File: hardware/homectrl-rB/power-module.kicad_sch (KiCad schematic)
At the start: 36 parts, among them J1 Barrel_Jack, Q1 DMP6023LE-13, U2 TPS5405DR, U3 ID_LM66100DCKR, U4 ID_LM66100DCKR

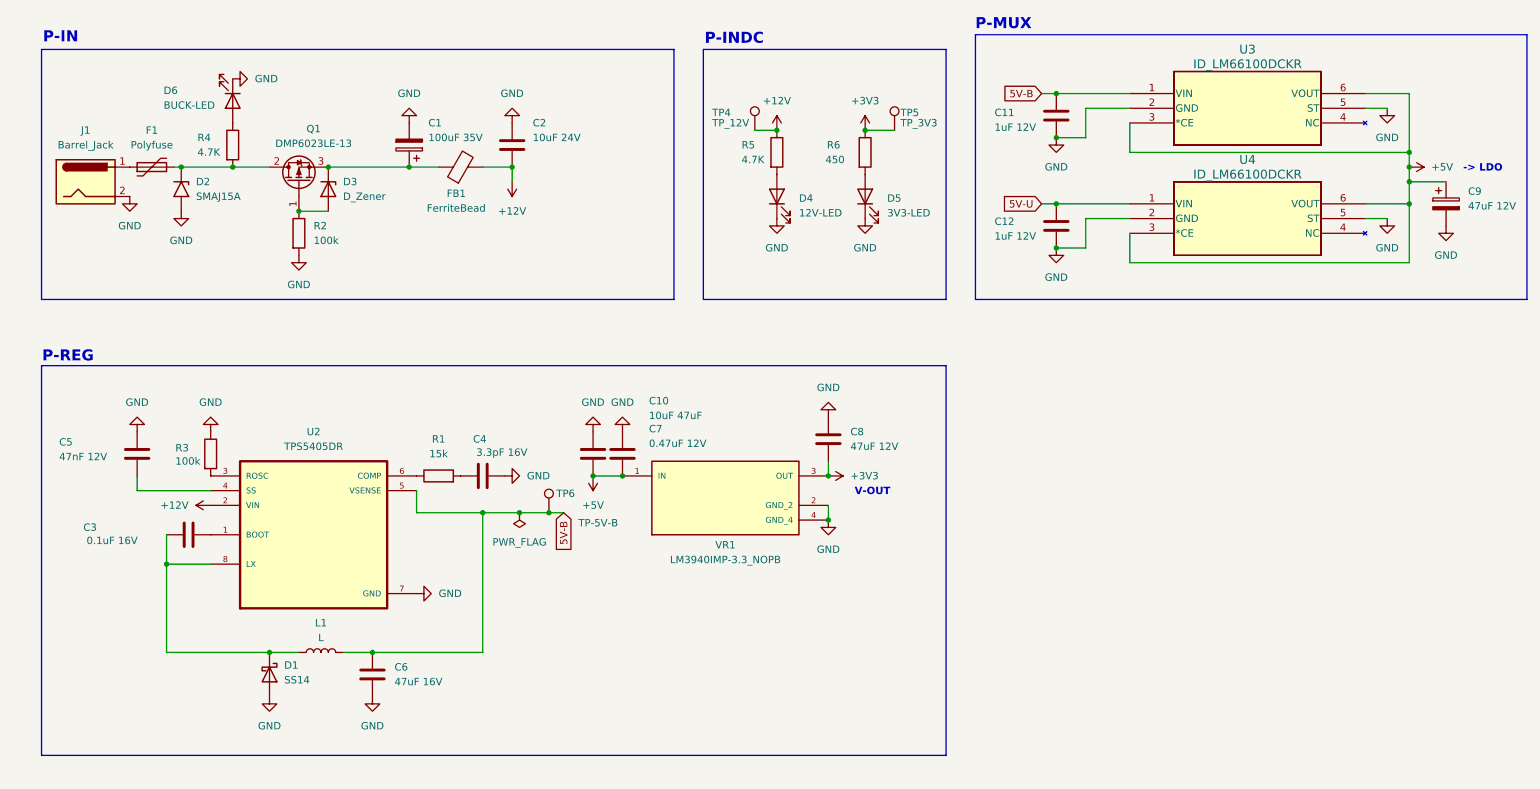
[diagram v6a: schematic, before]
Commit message: add MPNs and review circuits
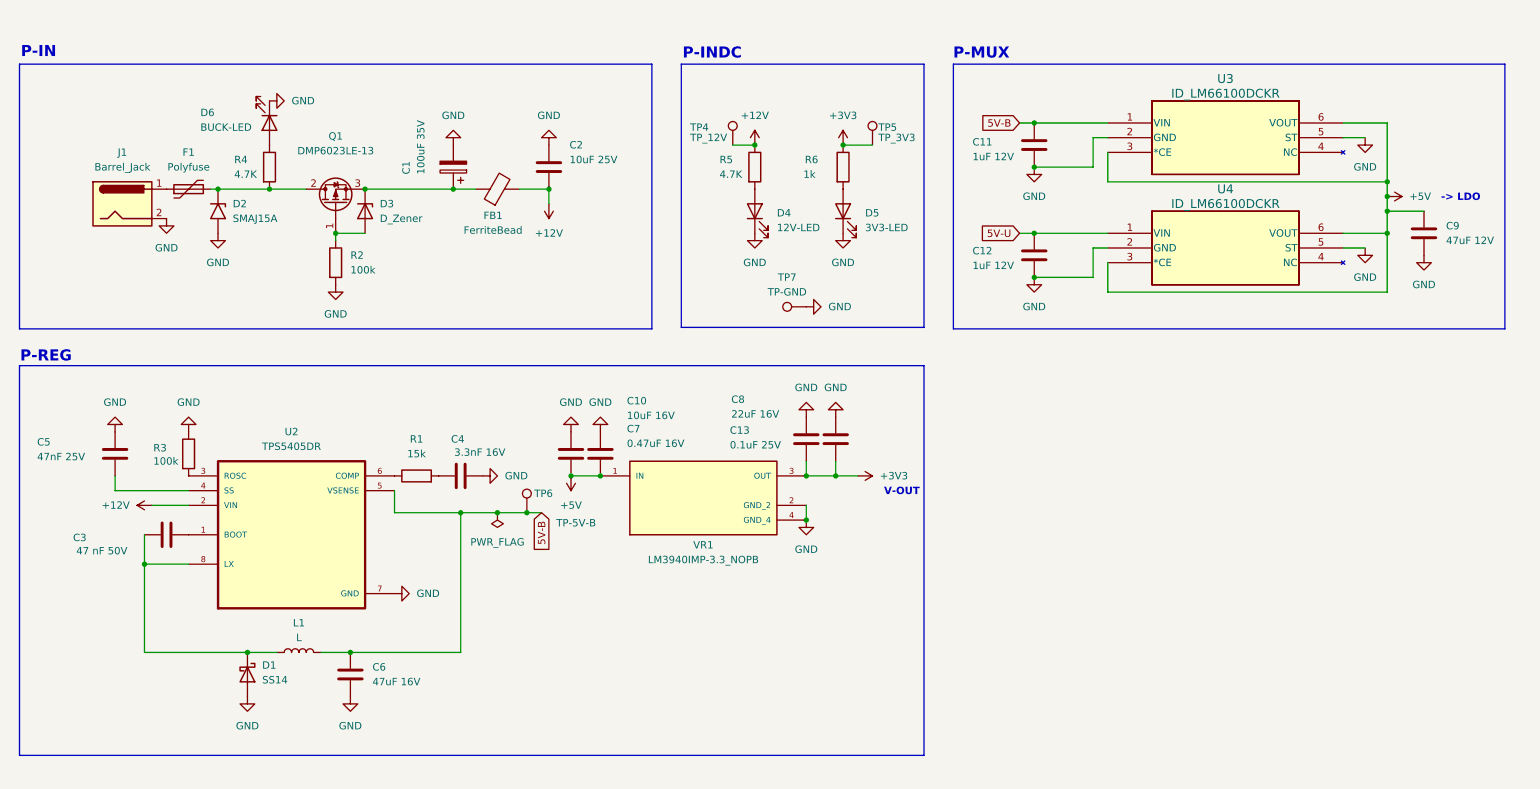
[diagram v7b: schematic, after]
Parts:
- added C13: 0.1uF 25V, Capacitor_SMD:C_0603_1608Metric, symbol Device:C
- added TP7: TP-GND, TestPoint:TestPoint_Pad_1.0x1.0mm, symbol Connector:TestPoint
- C10: value 10uF 47uF -> 10uF 16V; MPN (none) -> GRT188R61C106KE13D
- C11, C12: MPN (none) -> CL21B105KAFNNNE
- C2: value 10uF 24V -> 10uF 25V; MPN (none) -> CL21A106KAYNNNE
- C3: value 0.1uF 16V -> 47 nF 50V; MPN (none) -> GCM188R71H473KA55D
- C4: value 3.3pF 16V -> 3.3nF 16V; MPN (none) -> GRM155R71H332KA01D
- C5: value 47nF 12V -> 47nF 25V; MPN (none) -> GRM188R71H473KA61D
- C6: footprint Capacitor_SMD:C_0603_1608Metric -> Capacitor_SMD:C_0805_2012Metric; MPN (none) -> GRM21BR61A476ME15L
- C7: value 0.47uF 12V -> 0.47uF 16V; MPN (none) -> C1608X7R1C474K080AC
- C8: value 47uF 12V -> 22uF 16V; footprint Capacitor_SMD:C_0603_1608Metric -> Capacitor_SMD:C_0805_2012Metric; MPN (none) -> CL21A226MOQNNNE
- C9: footprint Capacitor_SMD:C_0603_1608Metric -> Capacitor_SMD:C_0805_2012Metric; symbol Device:C_Polarized -> Device:C; MPN (none) -> GRM21BR61A476ME15L
- D1: MPN SS14 -> SS24
- D3: footprint Diode_SMD:D_SOD-123F -> Diode_SMD:D_SOD-123; MPN (none) -> BZT52C12
- D4, D5: MPN (none) -> APT2012ZGCK
- D6: MPN (none) -> 150060GS75000
- F1: footprint 1210L110_16WR:FUSC3226X125N -> 0ZCG0260BF2B:FUSER_0ZCG0260BF2B; MPN 1210L110/16WR -> 0ZCG0260BF2B
- L1: footprint VLS3015CX-220M-1:IND_VLS3015CX-220M-1 -> IFSC1515AHER100M01:IND_IFSC_1515AH_VIS; MPN (none) -> IFSC1515AHER100M01
- R1: MPN (none) -> ERJ-2RKF1502X
- R2: MPN (none) -> ERJ-2RKF1003X
- R4, R5: MPN (none) -> ERJ-3EKF4701V
- R6: value 450 -> 1k; MPN (none) -> ERJ-2RKF1001X
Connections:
- net +3V3: now also C13.2
- net GND: now also C13.1, TP7.1
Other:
- moved on the sheet: C1, C10, C11, C12, C2, C3, C4, C5, C6, C7, C8, D1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

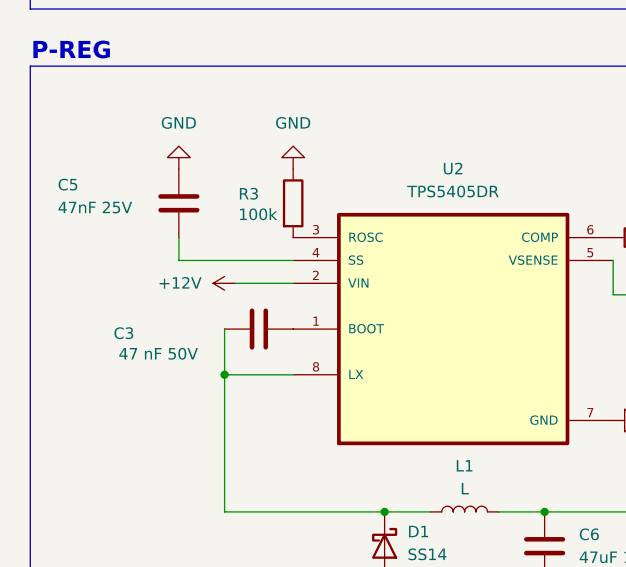
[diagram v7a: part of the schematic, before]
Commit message: review, add vias & ground pour
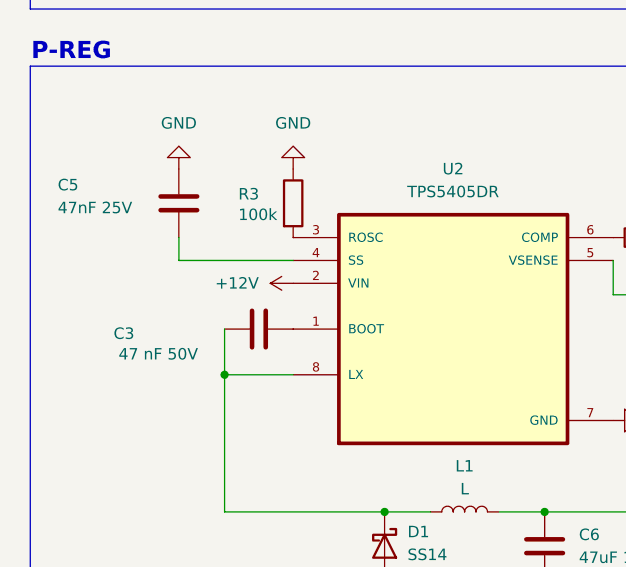
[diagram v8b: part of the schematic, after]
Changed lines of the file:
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@@
-	(wire
-		(pts
-			(xy 44.45 110.49) (xy 50.8 110.49)
-		)
-		(stroke
-			(width 0)
-			(type default)
-		)
-	)
 	(wire
 		(pts
@@
 	(symbol
 		(lib_id "power:+12V")
-		(at 44.45 110.49 90)
+		(at 50.8 110.49 90)
 		(unit 1)
 		(exclude_from_sim no)
@@
 		(fields_autoplaced yes)
 		(property "Reference" "#PWR010"
-			(at 48.26 110.49 0)
+			(at 54.61 110.49 0)
 			(effects
 				(font
@@
 		)
 		(property "Value" "+12V"
-			(at 40.64 110.4899 90)
+			(at 46.99 110.4899 90)
 			(effects
 				(font
@@
 		)
 		(property "Footprint" ""
-			(at 44.45 110.49 0)
+			(at 50.8 110.49 0)
 			(effects
 				(font
@@
 		)
 		(property "Datasheet" ""
-			(at 44.45 110.49 0)
+			(at 50.8 110.49 0)
 			(effects
 				(font
@@
 		)
 		(property "Description" "Power symbol creates a global label with name \"+12V\""
-			(at 44.45 110.49 0)
-			(effects
-				(font
+			(at 50.8 110.49 0)
+			(effects
+				(font
